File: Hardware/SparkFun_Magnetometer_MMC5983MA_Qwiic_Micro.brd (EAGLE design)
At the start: 7.6 x 19.1 mm, 35 parts, among them J1 QWIIC_RIGHT_ANGLE, U2 MMC5983MA_QFN16

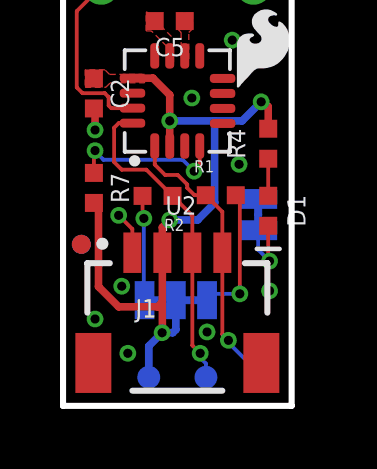
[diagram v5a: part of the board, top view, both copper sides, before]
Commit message: Adds measures, adds 0402 RED LED from lib
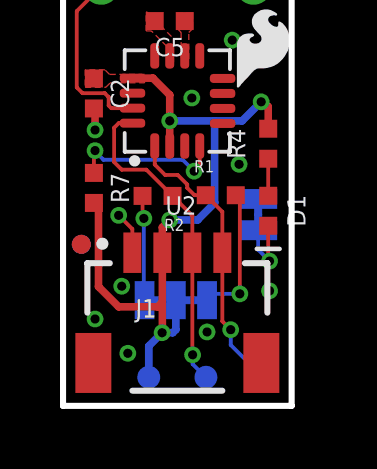
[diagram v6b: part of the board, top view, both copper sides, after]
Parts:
- added LOGO3: SFE_LOGO_NAMEBLANK, SparkFun-Aesthetics:BLANK
- D1: device ISM330DHCX:0402-TIGHT -> SparkFun-LED:LED-0402
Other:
- board text added: "Units in Inches"
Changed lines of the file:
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@@
 <drawing>
 <settings>
-<setting alwaysvectorfont="no"/>
+<setting alwaysvectorfont="yes"/>
 <setting keepoldvectorfont="yes"/>
 <setting verticaltext="up"/>
@@
 <layer number="45" name="Holes" color="7" fill="1" visible="yes" active="yes"/>
 <layer number="46" name="Milling" color="3" fill="1" visible="no" active="yes"/>
-<layer number="47" name="Measures" color="7" fill="1" visible="no" active="yes"/>
+<layer number="47" name="Measures" color="7" fill="1" visible="yes" active="yes"/>
 <layer number="48" name="Document" color="7" fill="1" visible="no" active="yes"/>
 <layer number="49" name="Reference" color="13" fill="1" visible="yes" active="yes"/>
@@
 <wire x1="6.0198" y1="9.045575" x2="6.0198" y2="8.537575" width="0.254" layer="22"/>
 <circle x="3.4925" y="8.78205" radius="0.5334" width="0.254" layer="22"/>
-<dimension x1="13.9446" y1="3.81" x2="13.97" y2="0" x3="25.4" y3="1.905" textsize="1.778" layer="47" dtype="vertical" unit="inch"/>
-<dimension x1="19.05" y1="7.62" x2="0" y2="7.62" x3="9.525" y3="16.764" textsize="1.778" layer="47" dtype="horizontal" unit="inch"/>
-<dimension x1="0" y1="7.62" x2="0" y2="0" x3="-6.096" y3="3.81" textsize="1.778" layer="47" dtype="horizontal" unit="inch"/>
-<dimension x1="8.89" y1="3.81" x2="0" y2="4.064" x3="4.445" y3="12.7" textsize="1.778" layer="47" dtype="horizontal" unit="inch"/>
-<dimension x1="2.54" y1="3.81" x2="0" y2="4.064" x3="1.27" y3="-3.302" textsize="1.778" layer="47" dtype="horizontal" unit="inch"/>
-<dimension x1="4.826" y1="1.016" x2="4.826" y2="0" x3="-1.27" y3="0.508" textsize="1.778" layer="47" dtype="vertical" unit="inch"/>
-<dimension x1="6.35" y1="1.016" x2="0" y2="1.016" x3="3.175" y3="-7.112" textsize="1.778" layer="47" unit="inch"/>
 <circle x="3.5052" y="8.7884" radius="0.2409625" width="0" layer="22"/>
+<dimension x1="1.27" y1="13.97" x2="0" y2="14.224" x3="0.635" y3="22.352" textsize="1.778" textratio="15" layer="47" dtype="horizontal" unit="inch"/>
+<dimension x1="1.27" y1="13.97" x2="2.032" y2="0" x3="-8.128" y3="6.985" textsize="1.778" textratio="15" layer="47" dtype="vertical" unit="inch"/>
+<dimension x1="7.62" y1="0" x2="7.62" y2="19.05" x3="17.145" y3="9.525" textsize="1.778" textratio="15" layer="47" dtype="horizontal" unit="inch"/>
+<dimension x1="0" y1="0" x2="7.62" y2="0" x3="3.81" y3="-8.5725" textsize="1.778" textratio="15" layer="47" dtype="horizontal" unit="inch"/>
+<dimension x1="3.81" y1="10.16" x2="0" y2="10.4775" x3="1.905" y3="26.67" textsize="1.778" textratio="15" layer="47" dtype="horizontal" unit="inch"/>
+<dimension x1="3.81" y1="10.16" x2="3.81" y2="0" x3="-3.81" y3="5.08" textsize="1.778" textratio="15" layer="47" dtype="horizontal" unit="inch"/>
+<dimension x1="1.27" y1="13.97" x2="6.35" y2="13.97" x3="3.81" y3="20.0025" textsize="1.778" textratio="15" layer="47" dtype="horizontal" unit="inch"/>
+<dimension x1="3.81" y1="5.1054" x2="7.62" y2="4.7625" x3="5.715" y3="-3.81" textsize="1.778" textratio="15" layer="47" dtype="horizontal" unit="inch"/>
+<text x="-27.6225" y="-6.6675" size="1.778" layer="47" font="vector" ratio="15">Units in Inches</text>
 </plain>
 <attributes>
@@
 <element name="FD2" library="SparkFun-Aesthetics" package="FIDUCIAL-MICRO" value="FIDUCIALUFIDUCIAL" x="0.6096" y="5.3848" smashed="yes" rot="MR90"/>
 <element name="LOGO1" library="SparkFun-Aesthetics" package="QWIIC_4MM" value="QWIIC_LOGO_4MM" x="0.9144" y="8.255" smashed="yes" rot="MR90"/>
-<element name="D1" library="ISM330DHCX" package="0402-TIGHT" value="RED" x="6.838340625" y="6.5024" smashed="yes" rot="R270">
+<element name="D1" library="SparkFun-LED" package="LED-0402" value="RED" x="6.838340625" y="6.5024" smashed="yes" rot="R270">
 <attribute name="NAME" x="7.473340625" y="6.5024" size="0.6096" layer="25" font="vector" ratio="20" rot="R270" align="bottom-center"/>
+<attribute name="PROD_ID" value="DIO-16757" x="6.838340625" y="6.5024" size="1.778" layer="27" rot="R270" display="off"/>
 <attribute name="VALUE" value="RED" x="6.203340625" y="6.5024" size="0.6096" layer="27" font="vector" ratio="20" rot="R270" align="top-center"/>
 </element>
@@
 </element>
 <element name="U$4" library="topMini" package="#LED#15" value="" x="6.5532" y="3.81" smashed="yes" rot="MR90"/>
+<element name="LOGO3" library="SparkFun-Aesthetics" package="BLANK" value="SFE_LOGO_NAMEBLANK" x="-39.0525" y="-20.955" smashed="yes"/>
 </elements>
 <signals>
@@
 <wire x1="3.056" y1="8.0438" x2="3.056" y2="8.662" width="0.127" layer="1"/>
 <wire x1="3.056" y1="8.0438" x2="3.4036" y2="7.6962" width="0.127" layer="1"/>
-<via x="5.5118" y="2.1844" extent="1-16" drill="0.3048"/>
-<wire x1="6.6675" y1="0.9525" x2="5.5118" y2="2.1082" width="0.127" layer="16"/>
-<wire x1="5.5118" y1="2.1844" x2="5.5118" y2="2.1082" width="0.127" layer="16"/>
-<wire x1="5.5118" y1="2.1844" x2="5.31" y2="2.3862" width="0.127" layer="1"/>
-<wire x1="5.31" y1="5.1054" x2="5.31" y2="2.3862" width="0.127" layer="1"/>
+<via x="5.588" y="2.54" extent="1-16" drill="0.3048"/>
+<wire x1="6.6675" y1="0.9525" x2="5.588" y2="2.032" width="0.127" layer="16"/>
+<wire x1="5.588" y1="2.54" x2="5.588" y2="2.032" width="0.127" layer="16"/>
+<wire x1="5.588" y1="2.54" x2="5.31" y2="2.818" width="0.127" layer="1"/>
+<wire x1="5.31" y1="5.1054" x2="5.31" y2="2.818" width="0.127" layer="1"/>
 <wire x1="4.1401" y1="7.37810625" x2="4.1401" y2="7.2645" width="0.127" layer="1"/>
 <wire x1="4.7578" y1="7.0216" x2="4.383" y2="7.0216" width="0.127" layer="1"/>
@@
 <wire x1="1.7018" y1="8.128" x2="1.9558" y2="7.874" width="0.127" layer="1"/>
 <wire x1="1.9558" y1="7.874" x2="2.7748" y2="7.874" width="0.127" layer="1"/>
-<wire x1="4.31" y1="5.1054" x2="4.31" y2="2.0146" width="0.127" layer="1"/>
-<wire x1="4.31" y1="2.0146" x2="4.572" y2="1.7526" width="0.127" layer="1"/>
-<via x="4.572" y="1.7526" extent="1-16" drill="0.3048"/>
-<wire x1="4.7625" y1="1.4097" x2="4.572" y2="1.6002" width="0.127" layer="16"/>
-<wire x1="4.572" y1="1.7526" x2="4.572" y2="1.6002" width="0.127" layer="16"/>
-<wire x1="4.7625" y1="1.4097" x2="4.7625" y2="0.9525" width="0.127" layer="16"/>
+<wire x1="4.31" y1="5.1054" x2="4.31" y2="1.7098" width="0.127" layer="1"/>
+<wire x1="4.31" y1="1.7098" x2="4.318" y2="1.7018" width="0.127" layer="1"/>
+<via x="4.318" y="1.7018" extent="1-16" drill="0.3048"/>
+<wire x1="4.318" y1="1.7018" x2="4.318" y2="1.397" width="0.127" layer="16"/>
+<wire x1="4.7625" y1="0.9525" x2="4.318" y2="1.397" width="0.127" layer="16"/>
 </signal>
 </signals>

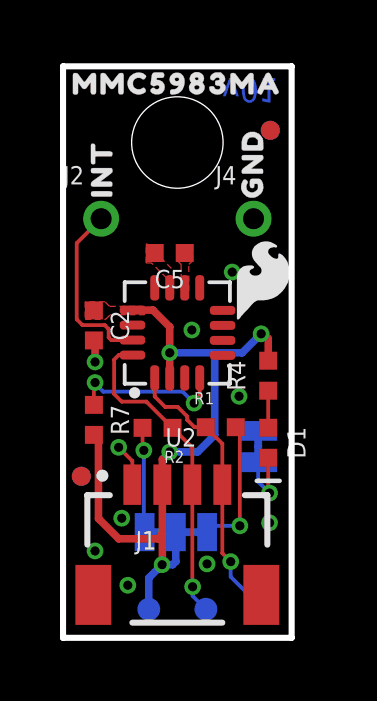
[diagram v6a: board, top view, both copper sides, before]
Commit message: Increases the size of the silk, fixes measures, rolls to version v10
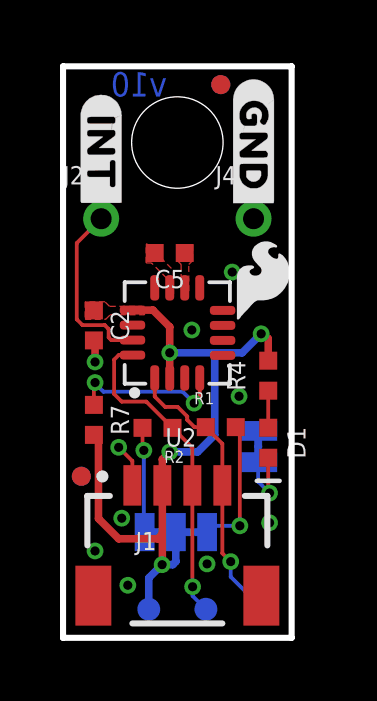
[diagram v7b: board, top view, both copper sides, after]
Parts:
- removed U$4: (no value), topMini:#LED#15
- added U$11: (no value), top:#LED#5
- added U$7: (no value), top:#GND#2
- U$1: device topMini:MMC5983MA331 -> top:#GND#0
- U$3: device LISMini:#I2C#7 -> top:#I2C#4
- U$5: device LISMini:GND4 -> top:#INT#1
- U$6: device LISMini:INT5 -> top:#INT#3
- moved LOGO2 8.03 mm to (6.07, 11.2), turned to 180 degrees
- moved U$5 5.06 mm to (1.27, 16.1), turned to 270 degrees
- moved U$3 3.30 mm to (3.81, 1.78), turned to 0 degrees
- moved U$1 3.28 mm to (6.35, 16.4), turned to 270 degrees
- moved FD1 2.25 mm to (5.26, 18.4)
- moved FID1 2.25 mm to (5.26, 18.4)
- moved U$6 0.49 mm to (1.27, 16.1), flipped to the bottom
- moved U$9 0.29 mm to (2.52, 10.4), turned to 0 degrees
- moved U$10 0.23 mm to (3.38, 7.42), turned to 0 degrees
- moved U$2 0.23 mm to (3.63, 12.8), turned to 0 degrees
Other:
- board text added: "v10"
- board text removed: "v01"

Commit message: Updates magnetometer symbol, moves I2C silk
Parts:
- removed U$7: (no value), top:#GND#2
- added U$4: (no value), top:#GND#4
- U$1: device top:#GND#0 -> top:#INT#20
- U$5: device top:#INT#1 -> top:#INT#21
- U$6: device top:#INT#3 -> top:#GND#4
- moved U$1 5.09 mm to (1.27, 16.1)
- moved U$6 5.09 mm to (6.35, 16.4)
- moved U$3 3.43 mm to (3.81, 5.21)
- moved U$8 1.52 mm to (4.95, 8.08)
- moved LOGO1 0.51 mm to (1.42, 8.26)
- moved LOGO2 0.34 mm to (5.87, 11.0), turned to 0 degrees
- moved U$11 0.13 mm to (6.48, 3.43)
- flipped U$5 to the bottom, turned to 90 degrees
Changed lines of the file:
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@@
 <setting verticaltext="up"/>
 </settings>
-<grid distance="0.0375" unitdist="inch" unit="inch" style="dots" multiple="1" display="yes" altdistance="0.005" altunitdist="inch" altunit="inch"/>
+<grid distance="0.05" unitdist="inch" unit="inch" style="dots" multiple="1" display="yes" altdistance="0.005" altunitdist="inch" altunit="inch"/>
 <layers>
 <layer number="1" name="Top" color="4" fill="1" visible="yes" active="yes"/>
@@
 <wire x1="0" y1="19.05" x2="0" y2="0" width="0.2032" layer="20"/>
 <wire x1="0" y1="0" x2="7.62" y2="0" width="0.2032" layer="20"/>
-<text x="3.463925" y="18.043525" size="0.8128" layer="16" font="vector" ratio="22" rot="SMR0">v10</text>
+<text x="0.219075" y="18.786475" size="0.8128" layer="16" font="vector" ratio="22" rot="SMR180">v10</text>
 <wire x1="6.2738" y1="8.791575" x2="4.3688" y2="8.791575" width="0.254" layer="22"/>
 <wire x1="6.2738" y1="8.791575" x2="6.0198" y2="8.537575" width="0.254" layer="22"/>
@@
 <attribute name="REV" value="" x="-18.796" y="-19.05" size="1.778" layer="27" display="off"/>
 </element>
-<element name="LOGO2" library="SparkFun-Aesthetics" package="OSHW-LOGO-MINI" value="OSHW-LOGOMINI" x="6.0706" y="11.24585" smashed="yes" rot="MR180"/>
+<element name="LOGO2" library="SparkFun-Aesthetics" package="OSHW-LOGO-MINI" value="OSHW-LOGOMINI" x="5.8674" y="10.97915" smashed="yes" rot="MR0"/>
 <element name="STANDOFF3" library="SparkFun-Hardware" package="STAND-OFF-TIGHT" value="STAND-OFFTIGHT" x="3.81" y="16.51" smashed="yes" rot="R270"/>
 <element name="R1" library="SparkFun-Resistors" package="0402-TIGHT" value="2.2k" x="5.2578" y="7.0216" smashed="yes">
@@
 <element name="FD1" library="SparkFun-Aesthetics" package="FIDUCIAL-MICRO" value="FIDUCIALUFIDUCIAL" x="5.2578" y="18.4404" smashed="yes" rot="MR90"/>
 <element name="FD2" library="SparkFun-Aesthetics" package="FIDUCIAL-MICRO" value="FIDUCIALUFIDUCIAL" x="0.6096" y="5.3848" smashed="yes" rot="MR90"/>
-<element name="LOGO1" library="SparkFun-Aesthetics" package="QWIIC_4MM" value="QWIIC_LOGO_4MM" x="0.9144" y="8.255" smashed="yes" rot="MR90"/>
+<element name="LOGO1" library="SparkFun-Aesthetics" package="QWIIC_4MM" value="QWIIC_LOGO_4MM" x="1.4224" y="8.255" smashed="yes" rot="MR90"/>
 <element name="D1" library="SparkFun-LED" package="LED-0402" value="RED" x="6.838340625" y="6.5024" smashed="yes" rot="R270">
 <attribute name="NAME" x="7.473340625" y="6.5024" size="0.6096" layer="25" font="vector" ratio="20" rot="R270" align="bottom-center"/>
@@
 </element>
 <element name="U$29" library="SparkFun-Aesthetics" package="SFE_LOGO_FLAME_.1" value="" x="6.6548" y="11.938" smashed="yes"/>
-<element name="U$8" library="ISMTopMini" package="X2114" value="" x="4.953" y="9.6012" smashed="yes" rot="MR0"/>
+<element name="U$8" library="ISMTopMini" package="X2114" value="" x="4.953" y="8.0772" smashed="yes" rot="MR0"/>
 <element name="U$9" library="ISMTopMini" package="Y2115" value="" x="2.525" y="10.3886" smashed="yes" rot="MR0"/>
 <element name="U$10" library="ISMTopMini" package="Z2116" value="" x="3.3782" y="7.4168" smashed="yes" rot="MR0"/>
@@
 </element>
 <element name="LOGO3" library="SparkFun-Aesthetics" package="BLANK" value="SFE_LOGO_NAMEBLANK" x="-39.0525" y="-20.955" smashed="yes"/>
-<element name="U$1" library="top" package="#GND#0" value="" x="6.35" y="16.383" smashed="yes" rot="R270"/>
-<element name="U$5" library="top" package="#INT#1" value="" x="1.27" y="16.129" smashed="yes" rot="R270"/>
-<element name="U$6" library="top" package="#INT#3" value="" x="1.27" y="16.129" smashed="yes" rot="MR90"/>
-<element name="U$7" library="top" package="#GND#2" value="" x="6.35" y="16.383" smashed="yes" rot="MR90"/>
-<element name="U$3" library="top" package="#I2C#4" value="" x="3.81" y="1.778" smashed="yes" rot="MR0"/>
-<element name="U$11" library="top" package="#LED#5" value="" x="6.604" y="3.429" smashed="yes" rot="MR90"/>
+<element name="U$3" library="top" package="#I2C#4" value="" x="3.81" y="5.207" smashed="yes" rot="MR0"/>
+<element name="U$11" library="top" package="#LED#5" value="" x="6.477" y="3.429" smashed="yes" rot="MR90"/>
+<element name="U$1" library="top" package="#INT#20" value="" x="1.27" y="16.129" smashed="yes" rot="R270"/>
+<element name="U$4" library="top" package="#GND#4" value="" x="6.35" y="16.383" smashed="yes" rot="R270"/>
+<element name="U$5" library="top" package="#INT#21" value="" x="1.27" y="16.129" smashed="yes" rot="MR90"/>
+<element name="U$6" library="top" package="#GND#4" value="" x="6.35" y="16.383" smashed="yes" rot="MR90"/>
 </elements>
 <signals>
